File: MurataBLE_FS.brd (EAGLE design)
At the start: 90 x 63 mm, 51 parts, among them CON2 C-2395.microSD, IC1 74LVC1G00DBV, IC2 IC_DCDC_LM27313, IC3 IC_LPC11U3XQFN33, IC4 IC_LDO_XX1117_4, IC5 IC_MEMORY_8P_AT25XE011_TSSOP, SW1 SW_TACTSW_2PP8073, SW2 SW_TACTSW_2PP8073, SW3 SW_TACTSW_2PP8073, U1 IC_BLE_LBCA2HNZYZ-711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

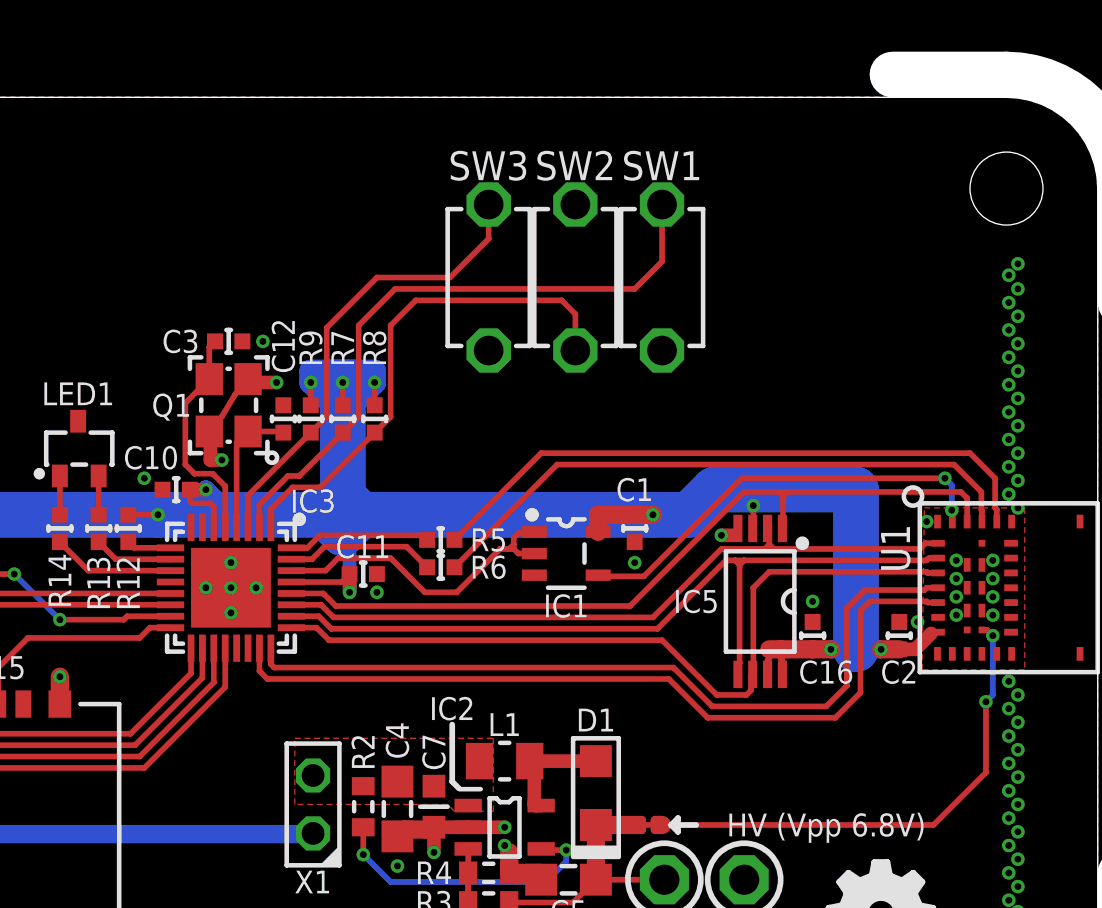
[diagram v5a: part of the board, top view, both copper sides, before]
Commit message: [ FS ] library update CON2/4; pin connection shift to avoid SWD pins
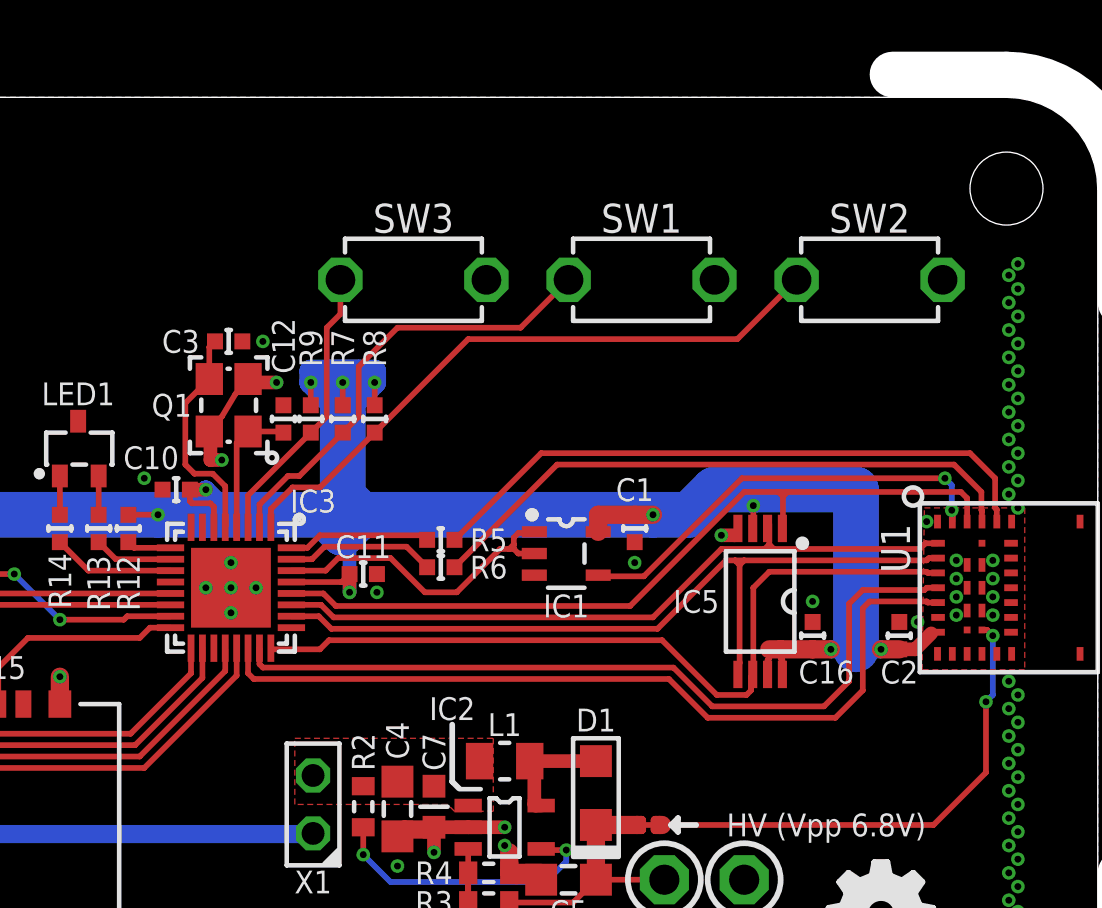
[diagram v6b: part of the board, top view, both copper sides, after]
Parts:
- CON1: value (none) -> WM17143CT-ND
- moved SW2 12.9 mm to (70.0, 45.0), turned to 180 degrees
- moved SW3 3.30 mm to (50.0, 45.0), turned to 180 degrees
- moved SW1 0.91 mm to (60.0, 45.0), turned to 180 degrees
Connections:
- net DETECT2: now also IC3.21; no longer IC3.20
- net MISO2: now also IC3.20; no longer IC3.19
- net SCK: now also IC3.24; no longer IC3.25
- net SWCLK: now also IC3.23; no longer IC3.24
- net SWDIO: now also IC3.22; no longer IC3.23
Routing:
- net !RESET!: track 27.9 -> 19.9 mm
- net ISP: track 20.4 -> 12.5 mm
- net BL: track 22.1 -> 28.0 mm
- net SCK: track 34.4 -> 35.3 mm
- net SWDIO: track 35.8 -> 36.4 mm
- net SWCLK: track 34.9 -> 35.4 mm

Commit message: [ FS ] library update
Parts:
- C8, C9: value 4.7u/1608 -> 4.7u/2012
- R5, R6: value 100/1005 -> 1k/1005
